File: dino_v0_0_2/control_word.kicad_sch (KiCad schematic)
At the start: 12 parts, among them U28 74LS138, U29 74LS138, U30 74LS138, U62 74LS02, U70 74LS138, U71 74LS138

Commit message: feat: Phase F/F+ ISA: 174 instructions, timing fixes, and robust tooling
This commit integrates Phase F and F+ of the ISA, expanding the instruction set to 174 instructions. This includes:
- New conditional branch `JNC`, register-to-register moves, SP/PC readbacks and manipulation (HLSP/SPHL, INXSP/DCXSP).
- Indexed memory access (LDAX/STAX), SP-relative memory access (LDAS/STAS), and memory-indirect addressing (LDAM/STAM/JMPM, etc.) as a new addressing mode.
- Immediate ALU operations (ADI, SUI, ANI, etc.) and ALU results directly to B/C or memory.
- Compare-only instructions (CMP, TST).
- The `IN` opcode has been fully retired from the ISA as of 2026-08-27, and `0x00` confirmed as `NOP`.

Crucially, this commit resolves several critical hardware stability issues:
- Eliminated random machine halts by replacing a damaged `74HC14` (`U56`) and rewiring the reset chain.
- Fixed intermittent failures in `PROG_isasoak` due to ground bounce by starring GND/VCC connections (2026-09-01).
- Introduced microcode-level "SETTLE" states for 23 ALU instructions to ensure timing margins at 1.024MHz, resolving timing-dependent failures for instructions that load and consume operands in consecutive T-states.

The development tooling has also been significantly improved for robustness and accuracy:
- The assembler (`asm.py`) now uses `microcode_gen.py` as the single source of truth for ISA definitions.
- New self-checking ISA tests (`PROG_isa` and variants) were developed, incorporating mutation testing to verify subtest efficacy and provide detailed diagnostic feedback for debugging marginality or hangs.
- The microcode generator enforces hardware constraints at build time (e.g., valid `cond` flag selections, preventing `src=ROM` `dst=RAM` conflicts that led to the `MVI` bug).
- The simulator (`progrom_gen.py`) accurately models `OUT` latching the bus and `dst=RAM` writing to the address bus, and refuses to guess undefined `FLAG_C` states after logic operations.
- The root `Makefile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
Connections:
- net FLAG_Z renamed COND_FLAG
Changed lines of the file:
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@@
 		)
 	)
-	(label "FLAG_Z"
+	(label "COND_FLAG"
 		(at 27.94 125.73 180)
 		(effects

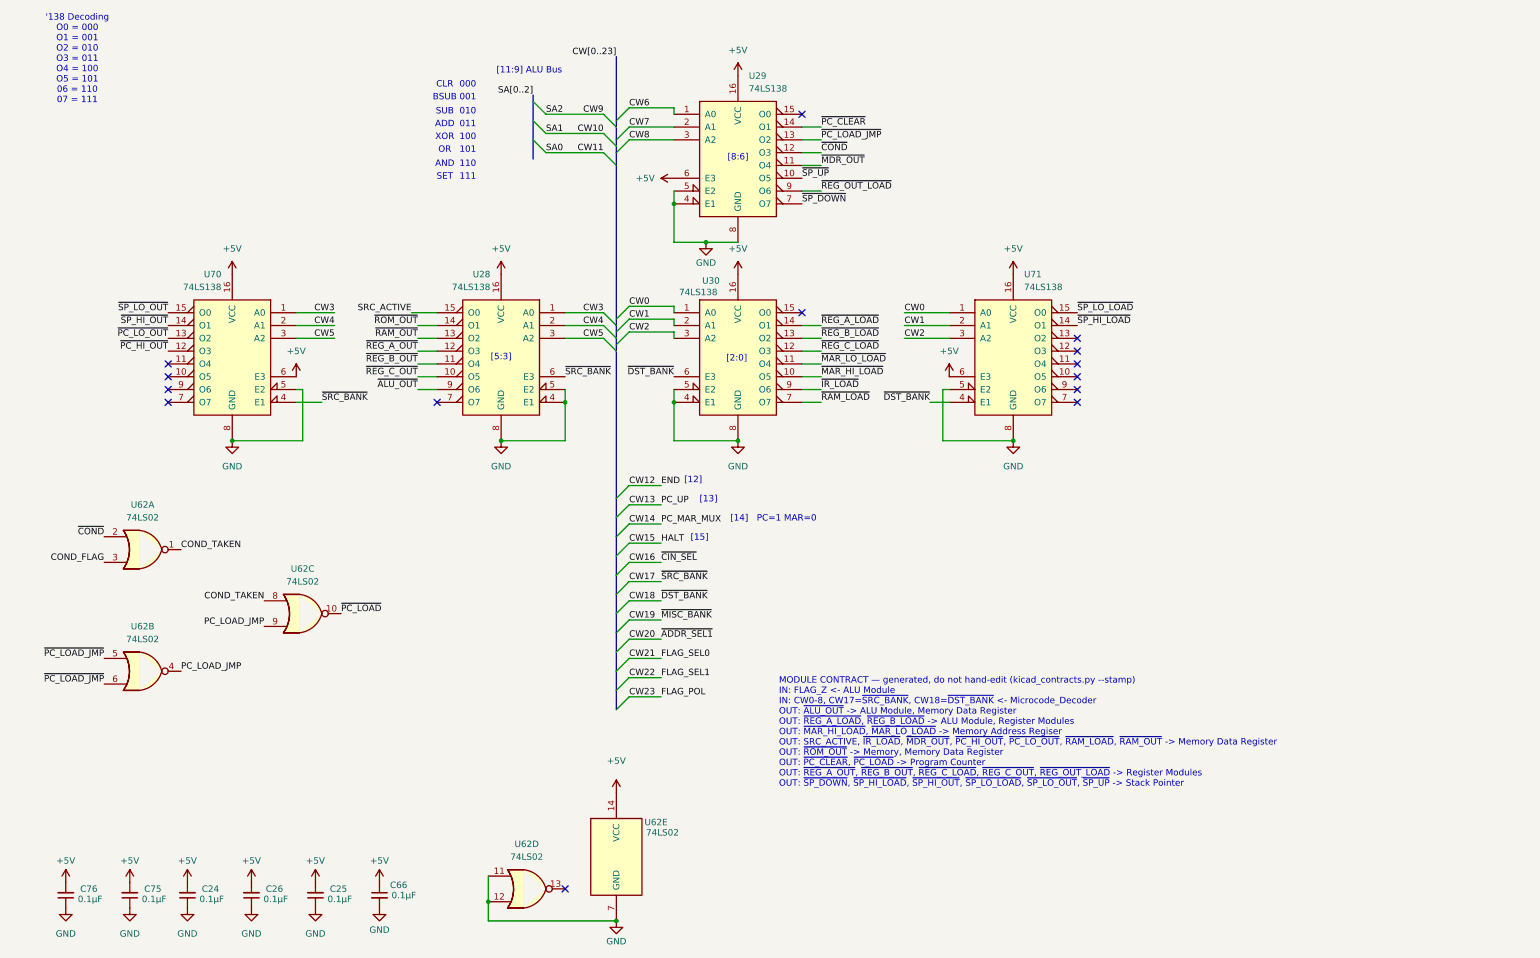
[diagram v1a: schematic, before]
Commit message: feat(kicad): footprints, power sheet, global labels, PCB draft
Every symbol gets a stock THT footprint (plain DIP, no sockets, so the
3D render shows ICs). New Power sheet: 24-pin ATX header for a picoPSU,
rails +5V/+3.3V/+12V/-12V/GND only; no -5V exists on any ATX unit since
2003, none drawn. PS_ON# on a 2-pin header.

Cross-sheet labels become global labels. KiCad joined nothing between
sheets before: 122 base names were split per sheet, ERC saw 90 undriven
inputs whose driver sat one sheet away, and the PCB ratsnest stopped at
every sheet boundary. Proof: KiCad's netlist after equals a name-join of
its netlist before plus the 15 CW alias pairs, pin for pin.

kicad_contracts took a node's sheet from the net name's /Sheet/ prefix;
global nets have none, so it emitted an empty contracts doc. Sheet now
comes from the component's own path; the doc regenerates with zero diff.

ERC 477 -> 2. Real fixes: ROM I/O pins input -> tri_state, '382 GND pin
power_out -> power_in, four orphan symbols rehomed to project lib `dino`,
one stub wire. 133 by-design warnings excluded by uuid ('245 readback on
counter Q, alias stubs, probe-point labels); the two left are bus
signals the peripheral bus sheet will consume.

PCB draft: 198 footprints placed per sheet, all pads netted, no tracks.

Co-Authored-By: Claude Fable 5.1 <noreply@anthropic.com>
Claude-Session: https://claude.ai/code/session_018irreFHb1xEykW5kCD26ow
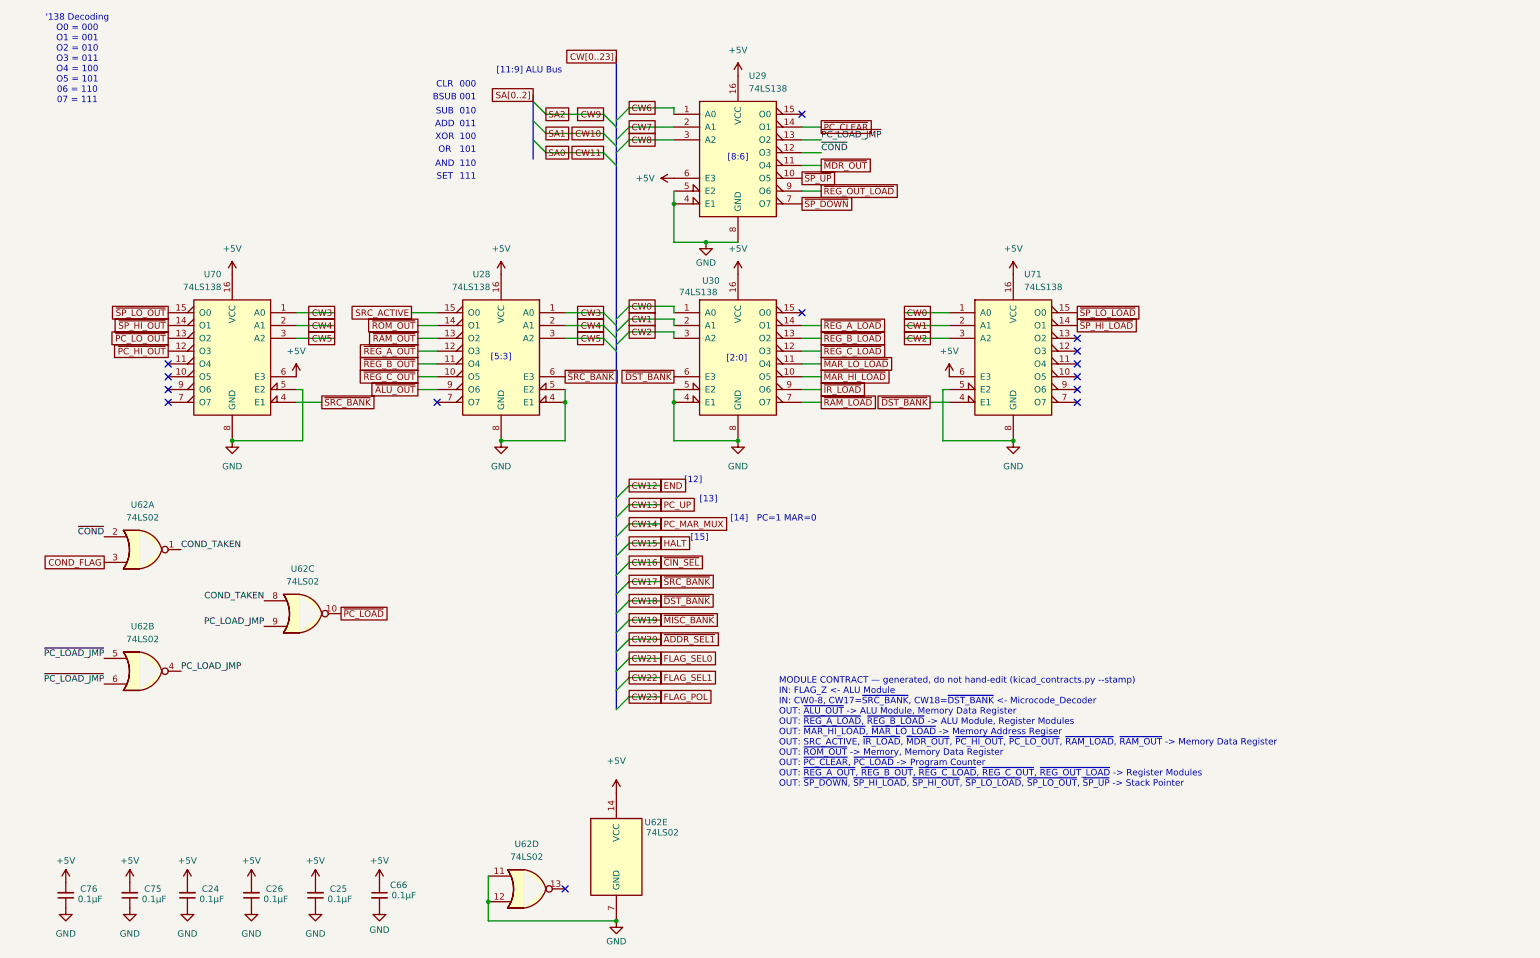
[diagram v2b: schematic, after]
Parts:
- C24, C25, C26, C66, C75, C76: footprint (none) -> Capacitor_THT:C_Disc_D5.0mm_W2.5mm_P2.50mm
- U28, U29, U30, U70, U71: footprint (none) -> Package_DIP:DIP-16_W7.62mm
- U62: footprint (none) -> Package_DIP:DIP-14_W7.62mm

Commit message: fix(copper): gate the RAM write strobe off in T-state 0; RAM-fetch halt closed
A RET fetched from RAM latched 0xFF. Scope work on 2026-09-29 found the
cause: the FETCH row's transparent IR moves the microcode EEPROM address
during CLK-low, the DST decoder (U30.7, code 111 = ~RAM_LOAD) runts for
14-16 ns on some opcode transitions, and NAND(WRITE_DIR, ~CLK) is open
then. The RAM got a 14 ns ~WE at PC's address; the cell survived, the
chip's read output did not, and IR latched 0xFF. From ROM the same runt
is harmless (M15 = 0). The same runt reached ~IO_WR and wrote 0x00 into
[MAR] at every RESET.

Fix: ~RAM_WRITE_EN = NAND(WRITE_DIR, WR_GATE), WR_GATE = NOR(CLK, ~TO0)
on U62 g4, with U56 3->4 inverting TO0 (U7.15). Drawn on control_word
(U62 g4), root (U56 sec 2) and memory (U51.4 label); ERC 0; six pins
beeped good against the drawing.

Witnesses: retlda 40/40 return (was 7/8 halting), no ~WE pulse under
59 ns in 10 runs on a pulse trigger, step2/retmvi/retcrlf/callret/
retinr/retldam/rethlsp 5/5 each, bigxfer returns, a planted byte at
0x8200 survives halt + RESET, and asm/ram/life.asm (Rule 30) runs to the
wall for the first time.

Docs: CLAUDE.md rewritten present-tense (facts only); every retraction
moved to .git/sdd/MISTAKES_MISSTEPS.md. test_ramret.py's table is marked
as the pre-gate record. RAM image headers stamped with the post-gate
result. dino_sheet_contracts.md regenerated by kicad_contracts.py.

Co-Authored-By: Claude Fable 5.1 <noreply@anthropic.com>
Claude-Session: https://claude.ai/code/session_01JGxSS4MVUcaZdKZGtKroSg
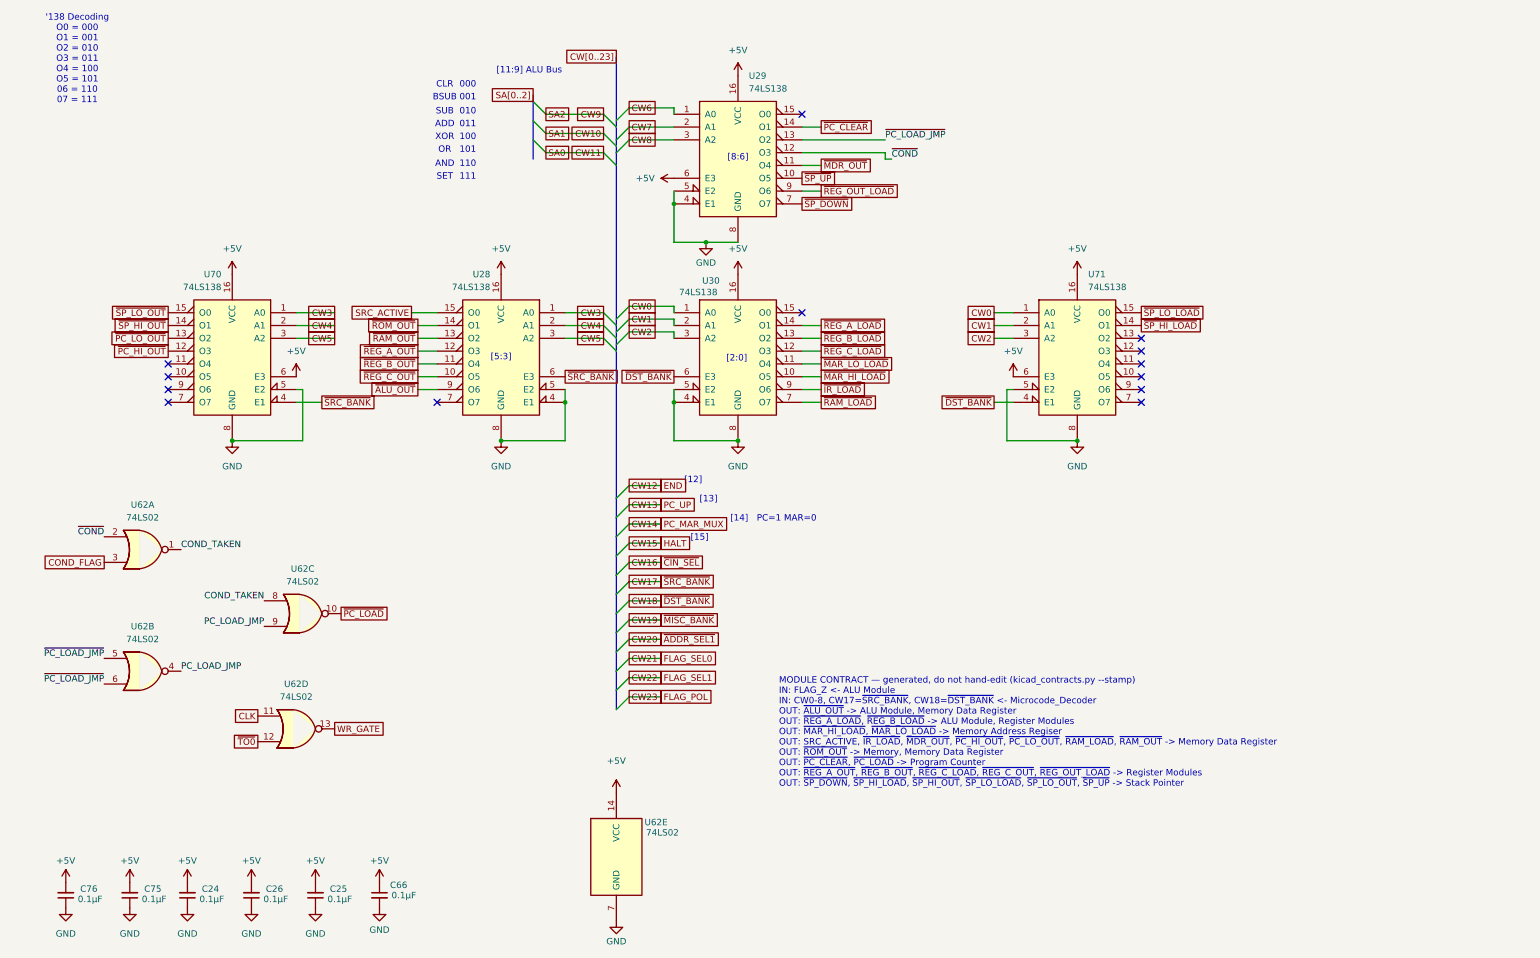
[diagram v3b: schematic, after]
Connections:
- net GND: no longer U62.11, U62.12
- net WR_GATE: now reaches U62.13
- new net CLK: U62.11
- new net ~{TO0}: U62.12
- no-connect marks 14 -> 13
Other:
- moved on the sheet: U62D, U71
